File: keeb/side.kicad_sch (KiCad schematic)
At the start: 62 parts, among them J1 USB_A, J3 USB_A, P1 USB_C_Plug_USB2.0, SW1 SW_Push, SW11 SW_Push, SW13 SW_Push, SW15 SW_Push, SW17 SW_Push, SW19 SW_Push, SW21 SW_Push, SW23 SW_Push, SW25 SW_Push, SW27 SW_Push, SW29 SW_Push, SW3 SW_Push, SW31 SW_Push, SW33 SW_Push, SW35 SW_Push, SW37 SW_Push, SW39 SW_Push, SW41 SW_Push, SW43 SW_Push, SW45 SW_Push, SW47 SW_Push, SW49 SW_Push, SW5 SW_Push, SW7 SW_Push, SW9 SW_Push, U1 XIAO-nRF52840-SMD, U3 USB2512-AEZG

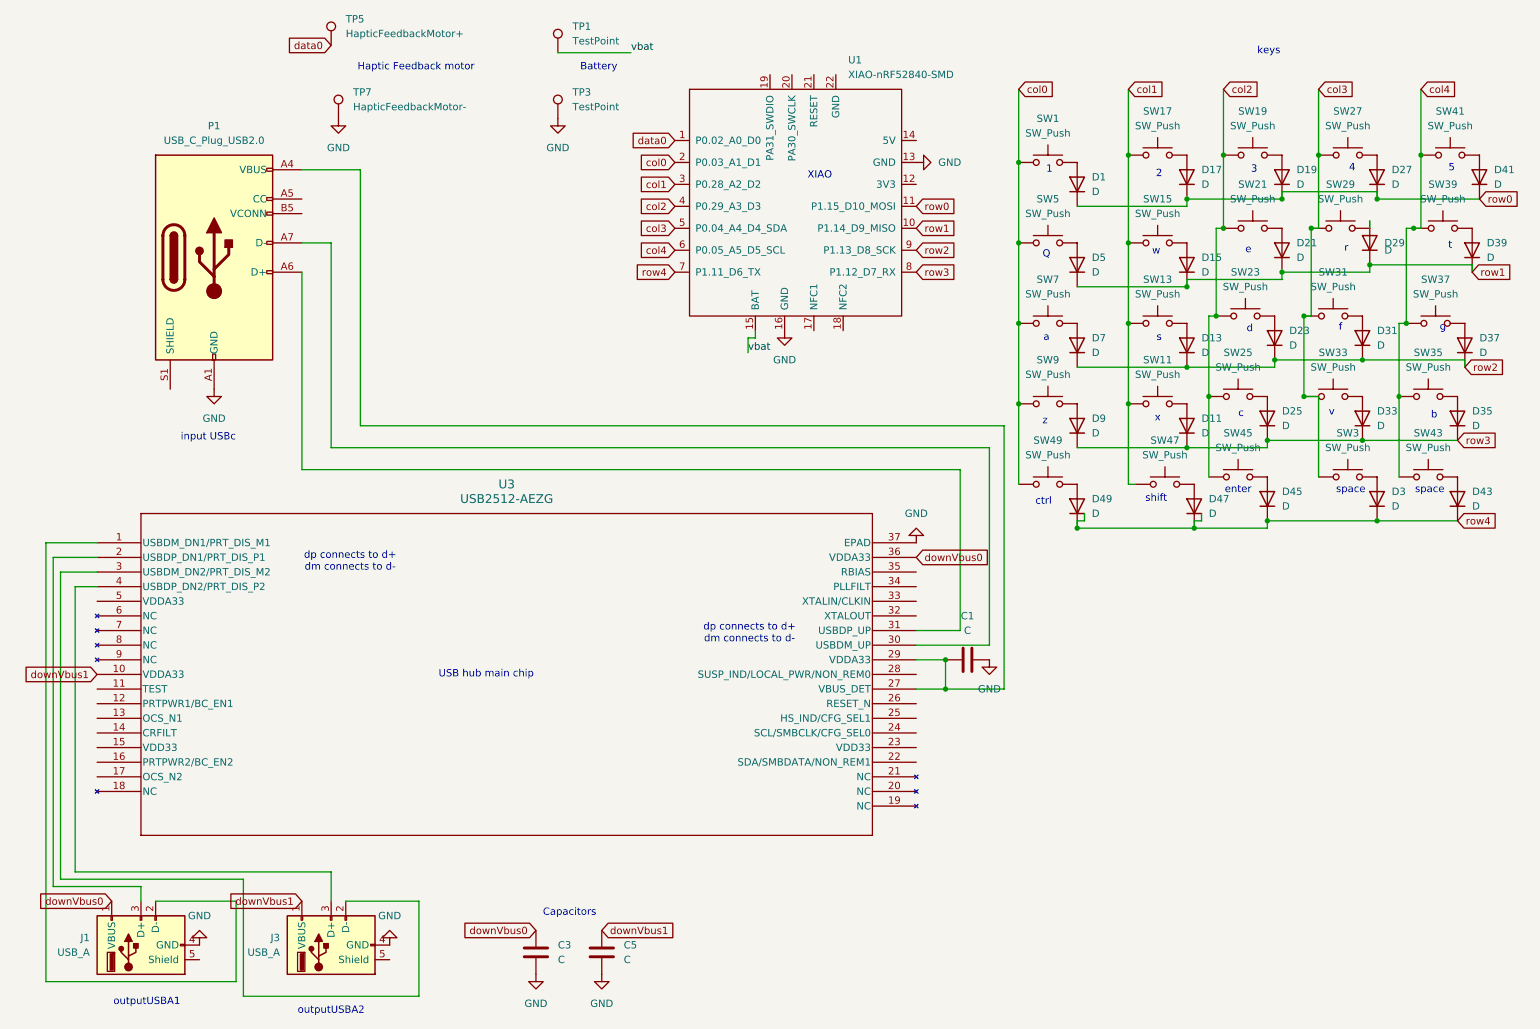
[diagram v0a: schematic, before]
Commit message: assigned footprints, fixed electrical rules checker errors
I fixed the ERC errors by adding no connect flags to the unused pins, I assigned the footprints for all the components, and initialized the PCB with all the components. I also forgot to add the mounting holes and mousebites to the last commit, so I added those as well. Next commit will be routing all the components, then full CAD, then firmware (looking to use KMK as that's what I used for the Macropad)
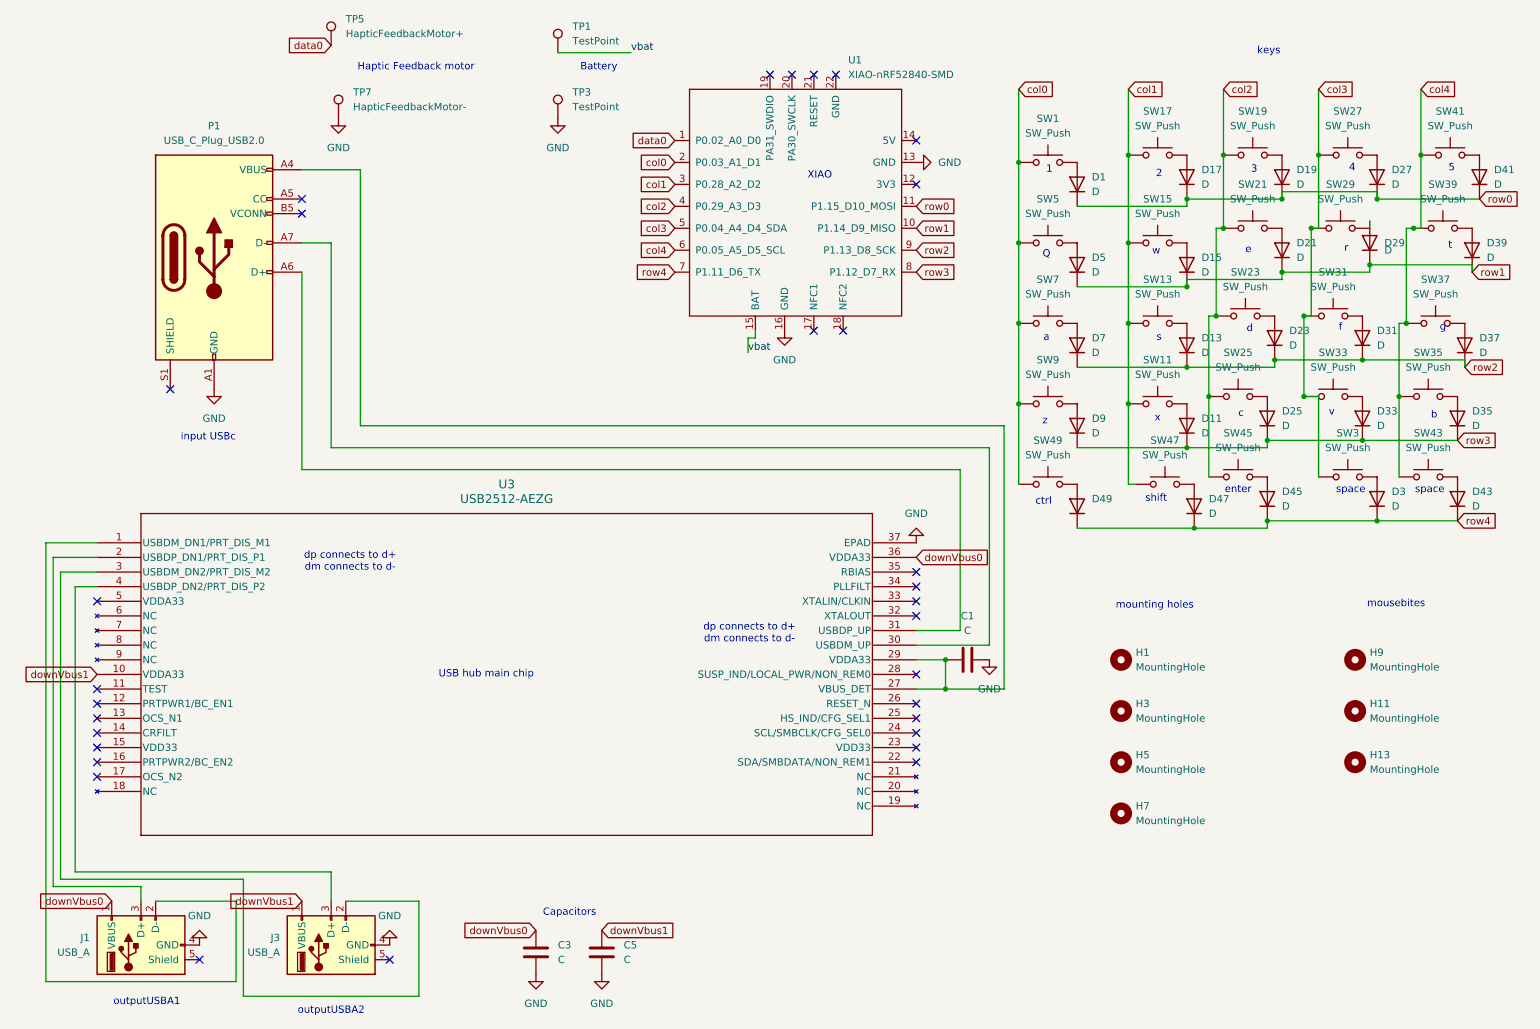
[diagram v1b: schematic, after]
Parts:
- added H1, H3, H5, H7: MountingHole, TestPoint:TestPoint_Loop_D3.80mm_Drill2.8mm, symbol Mechanical:MountingHole
- added H11, H13, H9: MountingHole, keeb:mouse-bite-5mm-slot, symbol Mechanical:MountingHole
- C1, C3, C5: footprint (none) -> Capacitor_THT:CP_Axial_L11.0mm_D8.0mm_P15.00mm_Horizontal
- D1, D11, D13, D15, D17, D19, D21, D23, D25, D27, D29, D3, D31, D33, D35, D37, D39, D41, D43, D45, D47, D49, D5, D7, D9: footprint (none) -> Diode_SMD:D_SOD-123
- J1, J3: footprint (none) -> Connector_USB:USB_A_Receptacle_GCT_USB1046
- P1: footprint (none) -> Connector_USB:USB_C_Plug_Molex_105444
- SW1, SW11, SW13, SW15, SW17, SW19, SW21, SW23, SW25, SW27, SW29, SW3, SW31, SW33, SW35, SW37, SW39, SW41, SW43, SW45, SW47, SW49, SW5, SW7, SW9: footprint (none) -> Button_Switch_Keyboard:SW_Cherry_MX_1.00u_PCB
- TP1, TP3: footprint (none) -> TestPoint:TestPoint_Pad_D3.0mm
- TP5, TP7: footprint (none) -> TestPoint:TestPoint_Pad_D4.0mm
- U1: footprint (none) -> keeb:modified-XIAO-nRF52840-SMD
- U3: footprint QFN36_6X6MC_MCH -> USB2512_AEZG:QFN36_6X6MC_MCH
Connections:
- no-connect marks 0 -> 31
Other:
- note added: "mounting holes"
- note added: "mousebites"
